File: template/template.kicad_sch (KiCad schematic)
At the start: 41 parts, among them J1 Network Connector, J2 B2B STLink connector, SW1 SW_Push, U1 LD39050PU33R, U2 STM32G474RBT6, U3 SN65HVD230, Y1 8MHz

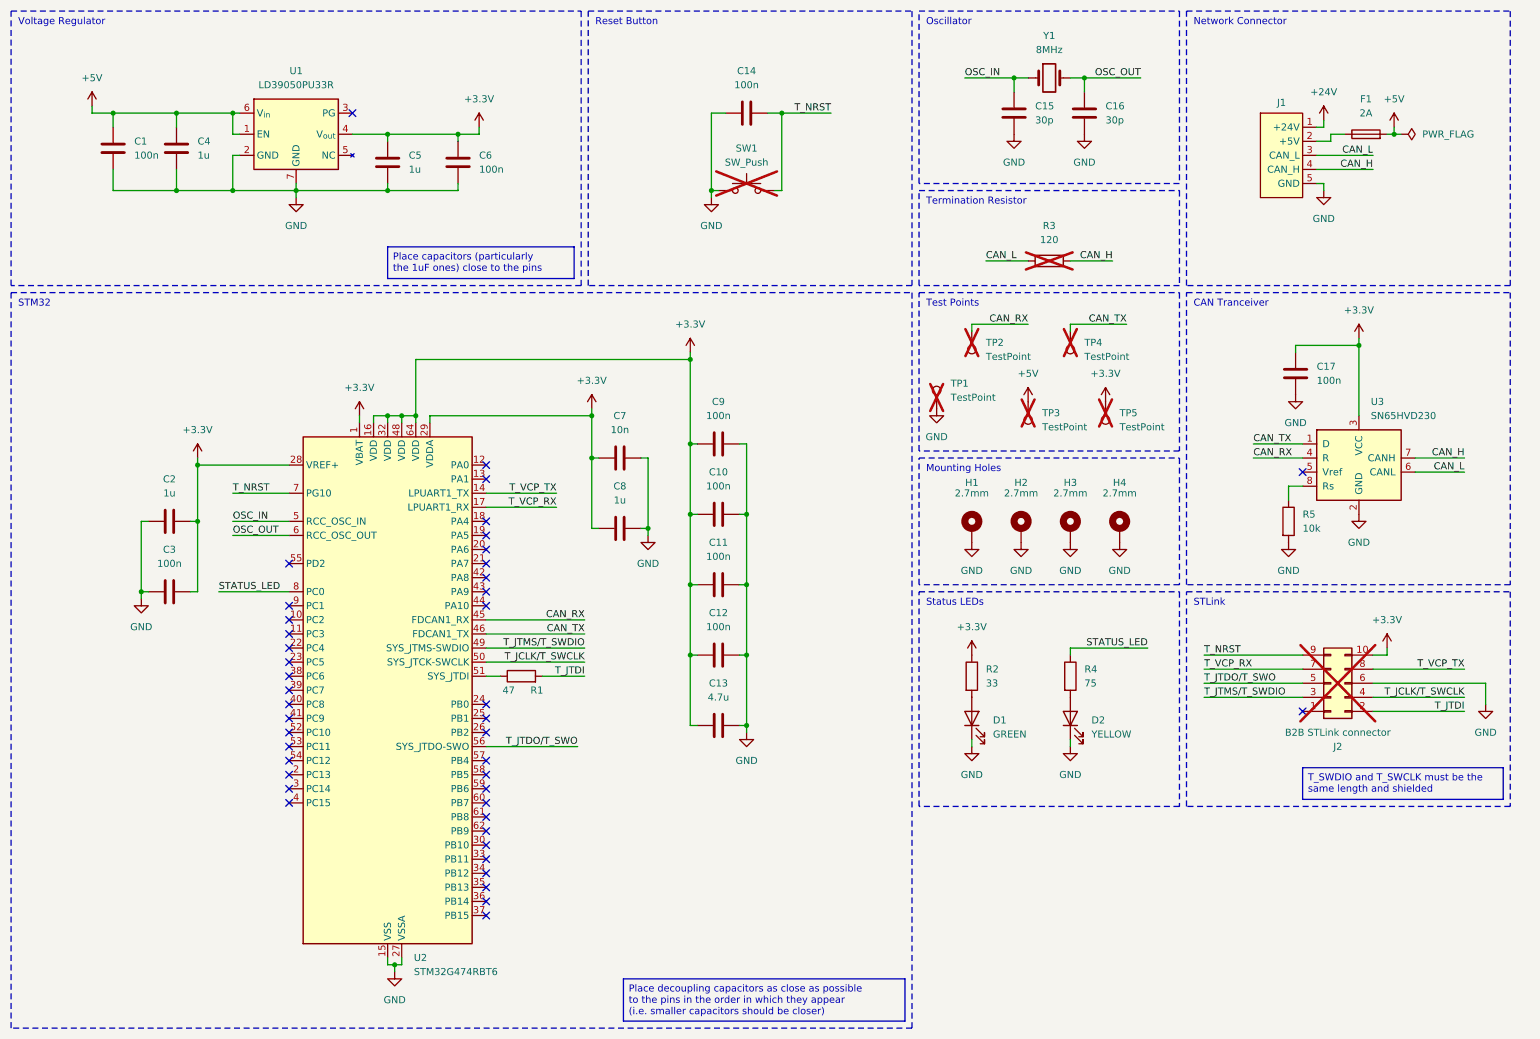
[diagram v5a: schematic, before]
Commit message: Move schematic to second page
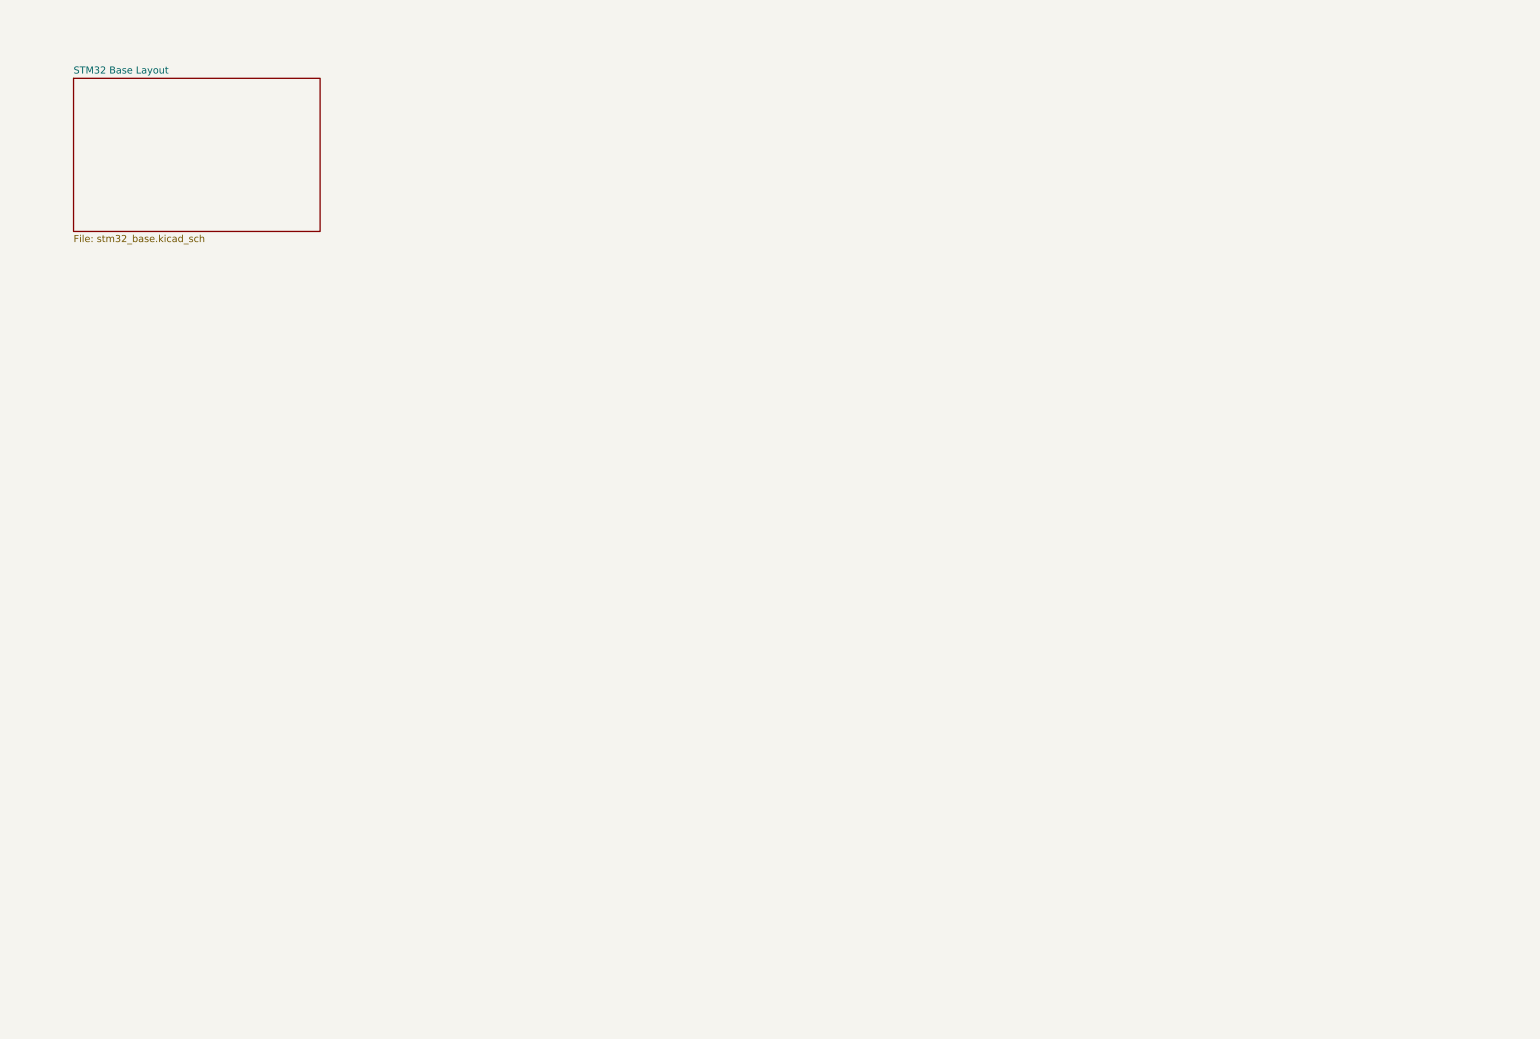
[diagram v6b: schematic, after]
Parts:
- removed C1, C10, C11, C12, C14, C17, C3, C6, C9: 100n, Capacitor_SMD:C_0402_1005Metric, symbol Device:C
- removed C13: 4.7u, Capacitor_SMD:C_0603_1608Metric, symbol Device:C
- removed C15, C16: 30p, Capacitor_SMD:C_0603_1608Metric, symbol Device:C
- removed C2, C4, C5, C8: 1u, Capacitor_SMD:C_0603_1608Metric, symbol Device:C
- removed C7: 10n, Capacitor_SMD:C_0603_1608Metric, symbol Device:C
- removed D1: GREEN, Exocet:LED_0805_2012Metric_With_Annotations, symbol Device:LED
- removed D2: YELLOW, Exocet:LED_0805_2012Metric_With_Annotations, symbol Device:LED
- removed F1: 2A, Exocet:Fuse_Holder_Littelfuse_01530008, symbol Device:Fuse
- removed H1, H2, H3, H4: 2.7mm, MountingHole:MountingHole_2.7mm_Pad, symbol Mechanical:MountingHole_Pad
- removed J1: Network Connector, Connector_Molex:Molex_SPOX_5268-05A_1x05_P2.50mm_Horizontal, symbol Exocet:Network_Connector
- removed J2: B2B STLink connector, Exocet:AVX 00-9159-010-BTB Connector, symbol Connector_Generic:Conn_02x05_Odd_Even
- removed R1: 47, Resistor_SMD:R_0603_1608Metric, symbol Device:R
- removed R2: 33, Resistor_SMD:R_0603_1608Metric, symbol Device:R
- removed R3: 120, Resistor_THT:R_Axial_DIN0309_L9.0mm_D3.2mm_P12.70mm_Horizontal, symbol Device:R
- removed R4: 75, Resistor_SMD:R_0603_1608Metric, symbol Device:R
- removed R5: 10k, Resistor_SMD:R_0603_1608Metric, symbol Device:R
- removed SW1: SW_Push, Button_Switch_THT:SW_PUSH_6mm, symbol Switch:SW_Push
- removed TP1, TP2, TP3, TP4, TP5: TestPoint, TestPoint:TestPoint_Keystone_5005-5009_Compact, symbol Connector:TestPoint
- removed U1: LD39050PU33R, Package_DFN_QFN:DFN-6-1EP_3x3mm_P0.95mm_EP1.7x2.6mm, symbol Exocet:LD39050PU33R
- removed U2: STM32G474RBT6, Package_QFP:LQFP-64_10x10mm_P0.5mm, symbol MCU_ST_STM32G4:STM32G474RBTx
- removed U3: SN65HVD230, Package_SO:SOIC-8_3.9x4.9mm_P1.27mm, symbol Interface_CAN_LIN:SN65HVD230
- removed Y1: 8MHz, Exocet:Crystal_SMD_HC49-SD, symbol Exocet:HSE_Oscillator
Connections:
- no-connect marks 43 -> 0
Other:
- added sheet STM32 Base Layout (stm32_base.kicad_sch)
- note removed: "CAN Tranceiver"
- note removed: "Mounting Holes"
- note removed: "Network Connector"
- note removed: "Oscillator"
- note removed: "Reset Button"
- note removed: "STLink"
- note removed: "STM32"
- note removed: "Status LEDs"
- note removed: "Termination Resistor"
- note removed: "Test Points"
- note removed: "Voltage Regulator"
- title: STM32 Base Layout -> (none)
